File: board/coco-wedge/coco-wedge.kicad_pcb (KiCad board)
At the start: 4 copper layers, 66 x 52.8 mm, 14 parts, among them J1 Foxconn_WQ21823-DES1-7F, U1 AMS1117-3.3, U2 STM32G0B0RETx, U3 74LVC1G07

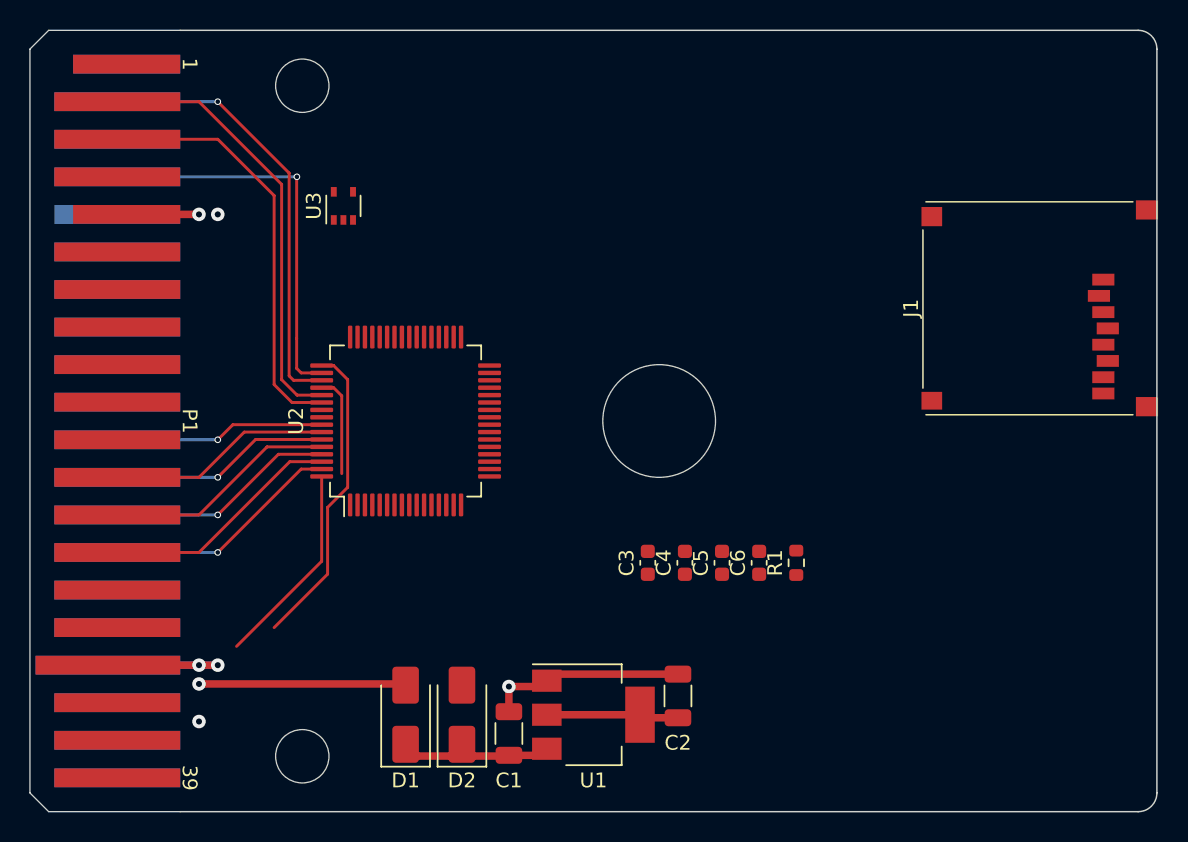
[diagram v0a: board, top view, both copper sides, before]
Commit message: Add most of the audio system, do some routing.
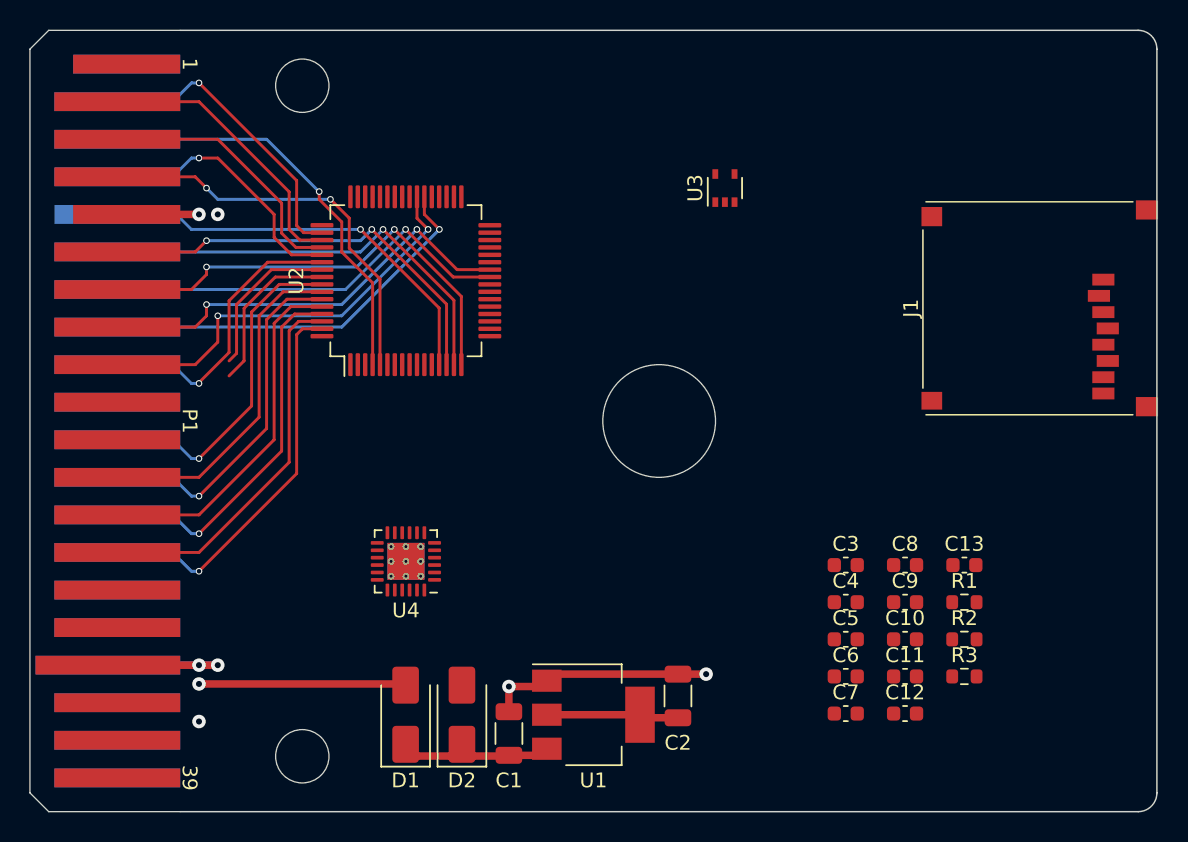
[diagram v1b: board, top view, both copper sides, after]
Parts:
- added C10: 1u, Capacitor_SMD:C_0603_1608Metric, F.Cu at (160.8, 116.4)
- added C11: 4u7, Capacitor_SMD:C_0603_1608Metric, F.Cu at (160.8, 118.9)
- added C12: 4u7, Capacitor_SMD:C_0603_1608Metric, F.Cu at (160.8, 121.4)
- added C13: 1u, Capacitor_SMD:C_0603_1608Metric, F.Cu at (164.8, 111.3)
- added C7: 4u7, Capacitor_SMD:C_0603_1608Metric, F.Cu at (156.8, 121.4)
- added C8: 4u7, Capacitor_SMD:C_0603_1608Metric, F.Cu at (160.8, 111.3)
- added C9: 4u7, Capacitor_SMD:C_0603_1608Metric, F.Cu at (160.8, 113.9)
- added R2: 100k, Resistor_SMD:R_0603_1608Metric, F.Cu at (164.8, 116.4)
- added R3: 100k, Resistor_SMD:R_0603_1608Metric, F.Cu at (164.8, 118.9)
- added U4: NAU8814Y, Package_DFN_QFN:VQFN-24-1EP_4x4mm_P0.5mm_EP2.5x2.5mm_ThermalVias, F.Cu at (127.0, 111.1)
- C5: value 100n -> 4u7
- C6: value 2u2 -> 100n
- moved U3 25.8 mm to (148.6, 85.9)
- moved C3 13.4 mm to (156.8, 111.3), turned to 0 degrees
- moved R1 11.7 mm to (164.8, 113.9), turned to 0 degrees
- moved C4 11.2 mm to (156.8, 113.9), turned to 0 degrees
- moved C5 9.84 mm to (156.8, 116.4), turned to 0 degrees
- moved C6 9.66 mm to (156.8, 118.9), turned to 0 degrees
- moved U2 9.49 mm to (127.0, 92.1)
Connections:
- P1 pad 35: unconnected-(P1-SND-Pad35) -> /SND
- U2 pad 1: /E -> /SD_MISO
- U2 pad 17: unconnected-(U2-PA0-Pad17) -> /I2S_BCLK
- U2 pad 18: unconnected-(U2-PA1-Pad18) -> /I2S_BCLK
- U2 pad 19: unconnected-(U2-PA2-Pad19) -> /I2S_OUT
- U2 pad 2: /Q -> /SD_MOSI
- U2 pad 20: unconnected-(U2-PA3-Pad20) -> /~{BOOT}
- U2 pad 21: /SD_~{CS} -> /I2S_FS
- U2 pad 22: /SD_SCLK -> /I2S_IN
- U2 pad 23: /SD_MISO -> /I2C_SDA
- U2 pad 24: /SD_MOSI -> /I2C_SCL
- U2 pad 36: unconnected-(U2-PA8-Pad36) -> /I2S_FS
- U2 pad 37: unconnected-(U2-PA9/NC-Pad37) -> /I2S_MCLK
- U2 pad 4: unconnected-(U2-PC14-Pad4) -> /E
- U2 pad 40: unconnected-(U2-PD8-Pad40) -> /~{SLEN}
- U2 pad 42: unconnected-(U2-PA10/NC-Pad42) -> /LED_B
- U2 pad 47: unconnected-(U2-PA15-Pad47) -> /SD_~{CS}
- U2 pad 48: /R/~{W} -> /LED_R
- U2 pad 49: /~{CTS} -> /LED_G
- U2 pad 5: unconnected-(U2-PC15-Pad5) -> /Q
- U2 pad 50: /~{CART} -> /~{NMI}
- U2 pad 51: /~{NMI} -> /~{HALT}
- U2 pad 52: /~{SLEN} -> /~{RESET}
- U2 pad 53: /~{HALT} -> /~{CART}
- U2 pad 54: /~{RESET} -> /R/~{W}
- U2 pad 55: unconnected-(U2-PD5-Pad55) -> /~{CTS}
- U2 pad 56: unconnected-(U2-PD6-Pad56) -> /~{SCS}
- U2 pad 64: /~{SCS} -> /SD_SCLK
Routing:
- net /D3: track 0.00 -> 31.7 mm, vias 0 -> 2
- net /D2: track 0.00 -> 29.7 mm, vias 0 -> 1
- net /D5: track 0.00 -> 29.5 mm, vias 0 -> 2
- net /D1: track 0.00 -> 29.1 mm, vias 0 -> 2
- net /D7: track 0.00 -> 28.4 mm, vias 0 -> 2
- net /E: track 0.00 -> 28.3 mm, vias 0 -> 1
- net /D0: track 0.00 -> 28.2 mm, vias 0 -> 1
- net /D4: track 0.00 -> 28.2 mm, vias 0 -> 1
- net /Q: track 0.00 -> 27.6 mm, vias 0 -> 2
- net /D6: track 0.00 -> 27.1 mm, vias 0 -> 1
- net /R/~{W}: track 0.00 -> 19.8 mm, vias 0 -> 1
- net /~{RESET}: track 28.7 -> 18.1 mm
- net /~{HALT}: track 29.8 -> 19.2 mm
- net /A9: track 16.2 -> 26.7 mm
- net /~{CTS}: track 21.0 -> 10.8 mm
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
